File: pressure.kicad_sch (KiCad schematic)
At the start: 15 parts, among them IC1 HSFPAR004A, U5 TLV9101IDBVR

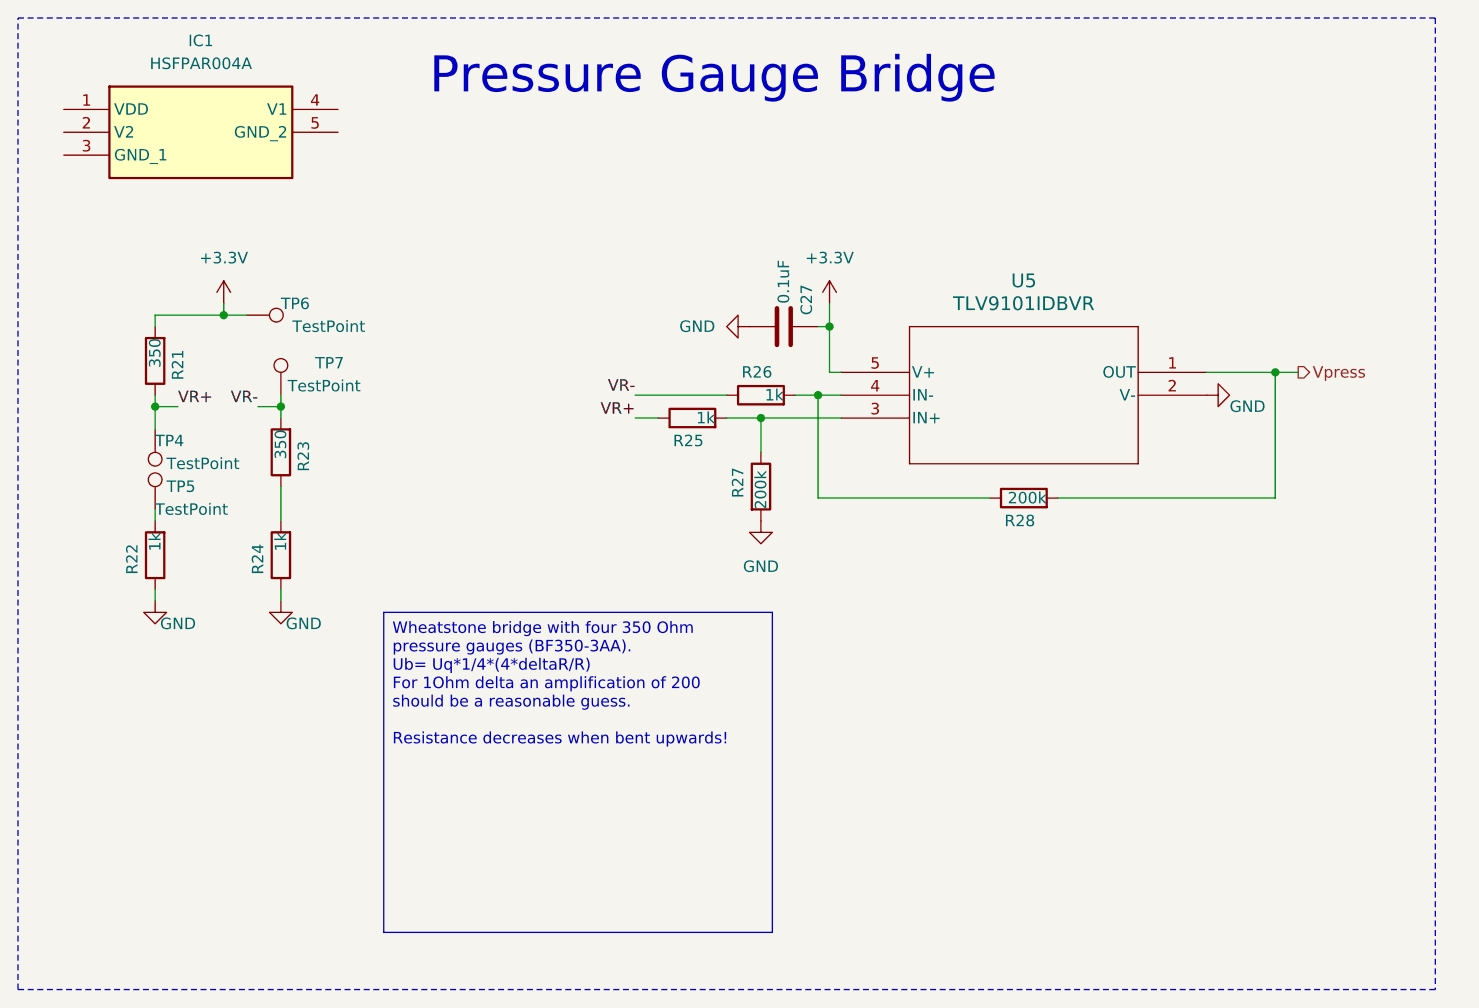
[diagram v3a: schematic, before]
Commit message: initial piezo resistive IC impl
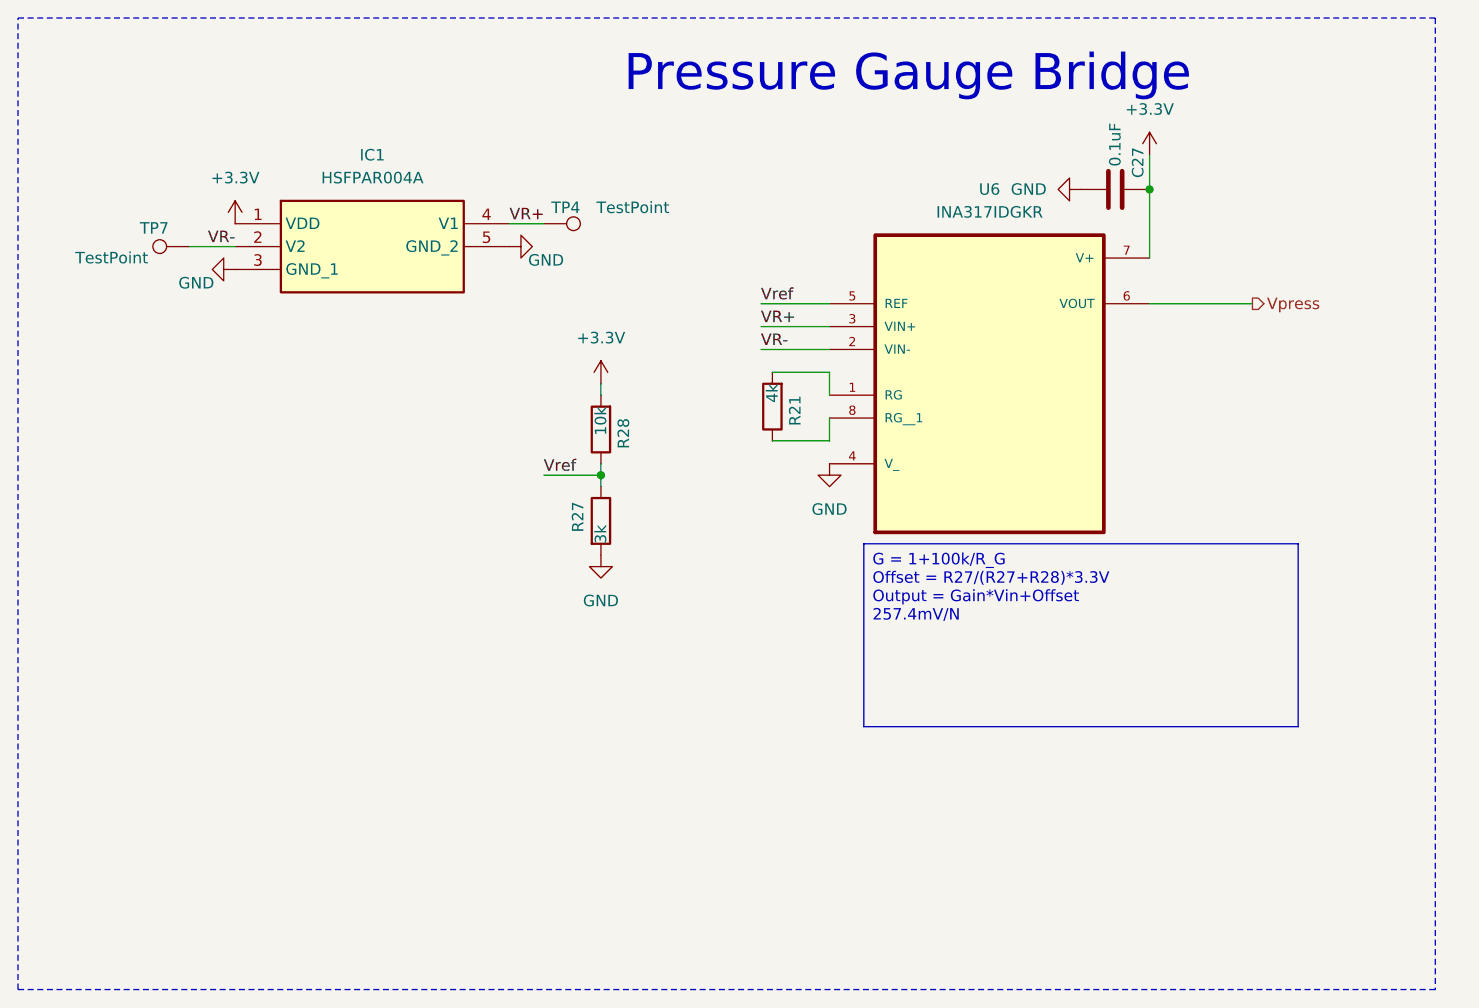
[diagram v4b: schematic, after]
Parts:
- removed R22, R24, R25, R26: 1k, Resistor_SMD:R_0805_2012Metric, symbol Device:R
- removed R23: 350, Resistor_SMD:R_0805_2012Metric, symbol Device:R
- removed TP5, TP6: TestPoint, TestPoint:TestPoint_Pad_D2.0mm, symbol Connector:TestPoint
- removed U5: TLV9101IDBVR, Snapeda:DBV0005A_TEX, symbol Snapeda:TLV9101IDBVR
- added U6: INA317IDGKR, Snapeda:INA317IDGKR_SOP65P490X110-8N, symbol Snapeda:INA317IDGKR
- R21: value 350 -> 4k
- R27: value 200k -> 3k
- R28: value 200k -> 10k
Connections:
- net +3.3V: now also IC1.1 (VDD), R28.2, U6.7 (V+); no longer R21.2
- net GND: now also IC1.3 (GND_1), IC1.5 (GND_2), U6.4 (V_)
- net VR+: now also IC1.4 (V1), U6.3 (VIN+); no longer R21.1
- net VR-: now also IC1.2 (V2), U6.2 (VIN-)
- net Vpress: now also U6.6 (VOUT); no longer R28.2
- net Vref: now reaches R27.1
- net Vref: now also R28.1, U6.5 (REF)
- new net: R21.1, U6.8 (RG__1)
- new net: R21.2, U6.1 (RG)
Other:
- moved on the sheet: C27, IC1, R27, R28, TP4, TP7

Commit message: continue new pressure sensor implementation
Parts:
- TP4, TP7: footprint TestPoint:TestPoint_Pad_D2.0mm -> TestPoint:TestPoint_Pad_D1.0mm
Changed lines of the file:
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@@
 			)
 		)
-		(property "Footprint" "TestPoint:TestPoint_Pad_D2.0mm"
+		(property "Footprint" "TestPoint:TestPoint_Pad_D1.0mm"
 			(at 44.45 40.64 0)
 			(effects
@@
 			)
 		)
-		(property "Footprint" "TestPoint:TestPoint_Pad_D2.0mm"
+		(property "Footprint" "TestPoint:TestPoint_Pad_D1.0mm"
 			(at 83.82 48.26 0)
 			(effects

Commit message: continue routing
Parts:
- added C30: 0.1uF, Capacitor_SMD:C_0805_2012Metric, symbol Device:C
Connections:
- net +3.3V: now also C30.1
- net GND: now also C30.2
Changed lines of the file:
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@@
+	)
+	(symbol
+		(lib_id "power:+3.3V")
+		(at 44.45 26.67 0)
+		(unit 1)
+		(exclude_from_sim no)
+		(in_bom yes)
+		(on_board yes)
+		(dnp no)
+		(property "Reference" "#PWR068"
+			(at 44.45 30.48 0)
+			(effects
+				(font
+					(size 1.27 1.27)
+				)
+				(hide yes)
+			)
+		)
+		(property "Value" "+3.3V"
+			(at 44.45 22.86 0)
+			(effects
+				(font
+					(size 1.27 1.27)
+				)
+			)
+		)
+		(property "Footprint" ""
+			(at 44.45 26.67 0)
+			(effects
+				(font
+					(size 1.27 1.27)
+				)
+				(hide yes)
+			)
+		)
+		(property "Datasheet" ""
+			(at 44.45 26.67 0)
+			(effects
+				(font
+					(size 1.27 1.27)
+				)
+				(hide yes)
+			)
+		)
+		(property "Description" "Power symbol creates a global label with name \"+3.3V\""
+			(at 44.45 26.67 0)
+			(effects
+				(font
+					(size 1.27 1.27)
+				)
+				(hide yes)
+			)
+		)
+		(pin "1"
+		)
+		(instances
+			(project "bierdeckel"
+				(path "/a4ffe097-37ef-4e19-a91a-ae57f4a5aad1/67cff1c4-a4ae-4e77-90c9-75aa7da1f628"
+					(reference "#PWR068")
+					(unit 1)
+				)
+			)
+		)
+	)
+	(symbol
+		(lib_id "power:GND")
+		(at 44.45 34.29 0)
+		(mirror y)
+		(unit 1)
+		(exclude_from_sim no)
+		(in_bom yes)
+		(on_board yes)
+		(dnp no)
+		(property "Reference" "#PWR069"
+			(at 44.45 40.64 0)
+			(effects
+				(font
+					(size 1.27 1.27)
+				)
+				(hide yes)
+			)
+		)
+		(property "Value" "GND"
+			(at 46.99 34.544 0)
+			(effects
+				(font
+					(size 1.27 1.27)
+				)
+			)
+		)
+		(property "Footprint" ""
+			(at 44.45 34.29 0)
+			(effects
+				(font
+					(size 1.27 1.27)
+				)
+				(hide yes)
+			)
+		)
+		(property "Datasheet" ""
+			(at 44.45 34.29 0)
+			(effects
+				(font
+					(size 1.27 1.27)
+				)
+				(hide yes)
+			)
+		)
+		(property "Description" "Power symbol creates a global label with name \"GND\" , ground"
+			(at 44.45 34.29 0)
+			(effects
+				(font
+					(size 1.27 1.27)
+				)
+				(hide yes)
+			)
+		)
+		(pin "1"
+		)
+		(instances
+			(project "bierdeckel"
+				(path "/a4ffe097-37ef-4e19-a91a-ae57f4a5aad1/67cff1c4-a4ae-4e77-90c9-75aa7da1f628"
+					(reference "#PWR069")
+					(unit 1)
+				)
+			)
+		)
 	)
 	(symbol
@@
 					(unit 1)
 				)
+			)
+		)
+	)
+	(symbol
+		(lib_id "Device:C")
+		(at 44.45 30.48 0)
+		(mirror y)
+		(unit 1)
+		(exclude_from_sim no)
+		(in_bom yes)
+		(on_board yes)
+		(dnp no)
+		(property "Reference" "C30"
+			(at 43.18 27.94 0)
+			(effects
+				(font
+					(size 1.27 1.27)
+				)
+				(justify left)
+			)
+		)
+		(property "Value" "0.1uF"
+			(at 41.91 30.48 0)
+			(effects
+				(font
+					(size 1.27 1.27)
+				)
+				(justify left)
+			)
+		)
+		(property "Footprint" "Capacitor_SMD:C_0805_2012Metric"
+			(at 43.4848 34.29 0)
+			(effects
+				(font
+					(size 1.27 1.27)
+				)
+				(hide yes)
+			)
+		)
+		(property "Datasheet" "~"
+			(at 44.45 30.48 0)
+			(effects
+				(font
+					(size 1.27 1.27)
+				)
+				(hide yes)
+			)
+		)
+		(property "Description" "Unpolarized capacitor"
+			(at 44.45 30.48 0)
+			(effects
+				(font
+					(size 1.27 1.27)
+				)
+				(hide yes)
+			)
+		)
+		(property "mpn" "KGM21NR71H104KT"
+			(at 44.45 30.48 0)
+			(effects
+				(font
+					(size 1.27 1.27)
+				)
+				(hide yes)
+			)
+		)
+		(pin "1"
+		)
+		(pin "2"
+		)
+		(instances
+			(project "bierdeckel"
+				(path "/a4ffe097-37ef-4e19-a91a-ae57f4a5aad1/67cff1c4-a4ae-4e77-90c9-75aa7da1f628"
+					(reference "C30")
+					(unit 1)
+				)

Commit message: continue refactor
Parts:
- removed TP4, TP7: TestPoint, TestPoint:TestPoint_Pad_D1.0mm, symbol Connector:TestPoint
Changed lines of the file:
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@@
+	(wire
+		(pts
+			(xy 83.82 43.18) (xy 80.01 43.18)
+		)
+		(stroke
+			(width 0)
+			(type default)
+		)
+	)
 	(wire
 		(pts
@@
 	(wire
 		(pts
-			(xy 83.82 43.18) (xy 80.01 43.18)
-		)
-		(stroke
-			(width 0)
-			(type default)
-		)
-	)
-	(wire
-		(pts
 			(xy 162.56 52.07) (xy 151.13 52.07)
 		)
@@
 	(wire
 		(pts
+			(xy 115.57 62.23) (xy 115.57 59.69)
+		)
+		(stroke
+			(width 0)
+			(type default)
+		)
+	)
+	(wire
+		(pts
+			(xy 115.57 67.31) (xy 109.22 67.31)
+		)
+		(stroke
+			(width 0)
+			(type default)
+		)
+	)
+	(wire
+		(pts
+			(xy 90.17 69.85) (xy 90.17 71.12)
+		)
+		(stroke
+			(width 0)
+			(type default)
+		)
+	)
+	(wire
+		(pts
+			(xy 83.82 71.12) (xy 90.17 71.12)
+		)
+		(stroke
+			(width 0)
+			(type default)
+		)
+	)
+	(wire
+		(pts
 			(xy 44.45 45.72) (xy 49.53 45.72)
-		)
-		(stroke
-			(width 0)
-			(type default)
-		)
-	)
-	(wire
-		(pts
-			(xy 115.57 62.23) (xy 115.57 59.69)
-		)
-		(stroke
-			(width 0)
-			(type default)
-		)
-	)
-	(wire
-		(pts
-			(xy 115.57 67.31) (xy 109.22 67.31)
-		)
-		(stroke
-			(width 0)
-			(type default)
-		)
-	)
-	(wire
-		(pts
-			(xy 90.17 69.85) (xy 90.17 71.12)
-		)
-		(stroke
-			(width 0)
-			(type default)
-		)
-	)
-	(wire
-		(pts
-			(xy 83.82 71.12) (xy 90.17 71.12)
 		)
 		(stroke
@@
 	)
 	(label "VR-"
-		(at 49.53 45.72 180)
+		(at 44.45 45.72 0)
 		(effects
 			(font
 				(size 1.27 1.27)
 			)
-			(justify right bottom)
+			(justify left bottom)
 		)
 	)
 	(label "VR+"
-		(at 80.01 43.18 0)
+		(at 83.82 43.18 180)
 		(effects
 			(font
 				(size 1.27 1.27)
 			)
-			(justify left bottom)
+			(justify right bottom)
 		)
 	)
@@
 	)
 	(symbol
-		(lib_id "Connector:TestPoint")
-		(at 44.45 45.72 90)
-		(unit 1)
-		(exclude_from_sim no)
-		(in_bom no)
-		(on_board yes)
-		(dnp no)
-		(property "Reference" "TP7"
-			(at 42.164 43.688 90)
-			(effects
-				(font
-					(size 1.27 1.27)
-				)
-				(justify left)
-			)
-		)
-		(property "Value" "TestPoint"
-			(at 39.878 46.99 90)
-			(effects
-				(font
-					(size 1.27 1.27)
-				)
-				(justify left)
-			)
-		)
-		(property "Footprint" "TestPoint:TestPoint_Pad_D1.0mm"
-			(at 44.45 40.64 0)
-			(effects
-				(font
-					(size 1.27 1.27)
-				)
-				(hide yes)
-			)
-		)
-		(property "Datasheet" "~"
-			(at 44.45 40.64 0)
-			(effects
-				(font
-					(size 1.27 1.27)
-				)
-				(hide yes)
-			)
-		)
-		(property "Description" "test point"
-			(at 44.45 45.72 0)
-			(effects
-				(font
-					(size 1.27 1.27)
-				)
-				(hide yes)
-			)
-		)
-		(property "mpn" ""
-			(at 44.45 45.72 0)
-			(effects
-				(font
-					(size 1.27 1.27)
-				)
-				(hide yes)
-			)
-		)
-		(pin "1"
-		)
-		(instances
-			(project "bierdeckel"
-				(path "/a4ffe097-37ef-4e19-a91a-ae57f4a5aad1/67cff1c4-a4ae-4e77-90c9-75aa7da1f628"
-					(reference "TP7")
-					(unit 1)
-				)
-			)
-		)
-	)
-	(symbol
 		(lib_id "power:GND")
 		(at 90.17 80.01 0)
@@
 		)
 		(instances
-			(project ""
+			(project "bierdeckel"
 				(path "/a4ffe097-37ef-4e19-a91a-ae57f4a5aad1/67cff1c4-a4ae-4e77-90c9-75aa7da1f628"
 					(reference "U6")
@@
 	)
 	(symbol
-		(lib_id "Connector:TestPoint")
-		(at 83.82 43.18 270)
-		(unit 1)
-		(exclude_from_sim no)
-		(in_bom no)
-		(on_board yes)
-		(dnp no)
-		(property "Reference" "TP4"
-			(at 87.884 41.402 90)
-			(effects
-				(font
-					(size 1.27 1.27)
-				)
-				(justify right)
-			)
-		)
-		(property "Value" "TestPoint"
-			(at 97.79 41.402 90)
-			(effects
-				(font
-					(size 1.27 1.27)
-				)
-				(justify right)
-			)
-		)
-		(property "Footprint" "TestPoint:TestPoint_Pad_D1.0mm"
-			(at 83.82 48.26 0)
-			(effects
-				(font
-					(size 1.27 1.27)
-				)
-				(hide yes)
-			)
-		)
-		(property "Datasheet" "~"
-			(at 83.82 48.26 0)
-			(effects
-				(font
-					(size 1.27 1.27)
-				)
-				(hide yes)
-			)
-		)
-		(property "Description" "test point"
-			(at 83.82 43.18 0)
-			(effects
-				(font
-					(size 1.27 1.27)
-				)
-				(hide yes)
-			)
-		)
-		(property "mpn" ""
-			(at 83.82 43.18 0)
-			(effects
-				(font
-					(size 1.27 1.27)
-				)
-				(hide yes)
-			)
-		)
-		(pin "1"
-		)
-		(instances
-			(project "bierdeckel"
-				(path "/a4ffe097-37ef-4e19-a91a-ae57f4a5aad1/67cff1c4-a4ae-4e77-90c9-75aa7da1f628"
-					(reference "TP4")
-					(unit 1)
-				)
-			)
-		)
-	)
-	(symbol
 		(lib_id "power:+3.3V")
 		(at 49.53 43.18 0)
@@
 		)
 		(instances
-			(project ""
+			(project "bierdeckel"
 				(path "/a4ffe097-37ef-4e19-a91a-ae57f4a5aad1/67cff1c4-a4ae-4e77-90c9-75aa7da1f628"
 					(reference "IC1")

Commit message: further work
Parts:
- added C31: 0.1uF, Capacitor_SMD:C_0603_1608Metric, symbol Device:C
- added R22: 4k, Resistor_SMD:R_0603_1608Metric, symbol Device:R
- C27, C30: footprint Capacitor_SMD:C_0805_2012Metric -> Capacitor_SMD:C_0603_1608Metric
- R21, R27, R28: footprint Resistor_SMD:R_0805_2012Metric -> Resistor_SMD:R_0603_1608Metric
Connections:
- net GND: now also C31.2
- net Vpress: now also C31.1, R22.1; no longer U6.6 (VOUT)
- new net: R22.2, U6.6 (VOUT)
